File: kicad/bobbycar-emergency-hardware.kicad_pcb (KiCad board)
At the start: 2 copper layers, 40 x 90 mm, 44 parts, among them J1 CAN2, J2 PROG, Q1 SS8050_C2150, Q2 SS8050_C2150, SW1 ANALOG_LEFT, U1 SN65HVD231, U2 ESP32-WROOM-32, U3 AMS1117-3.3, U4 MPM2359, U5 CH343G

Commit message: PCB Files and more screenshots
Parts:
- removed G***: LOGO, Logo:lenas_bobbycar_logo

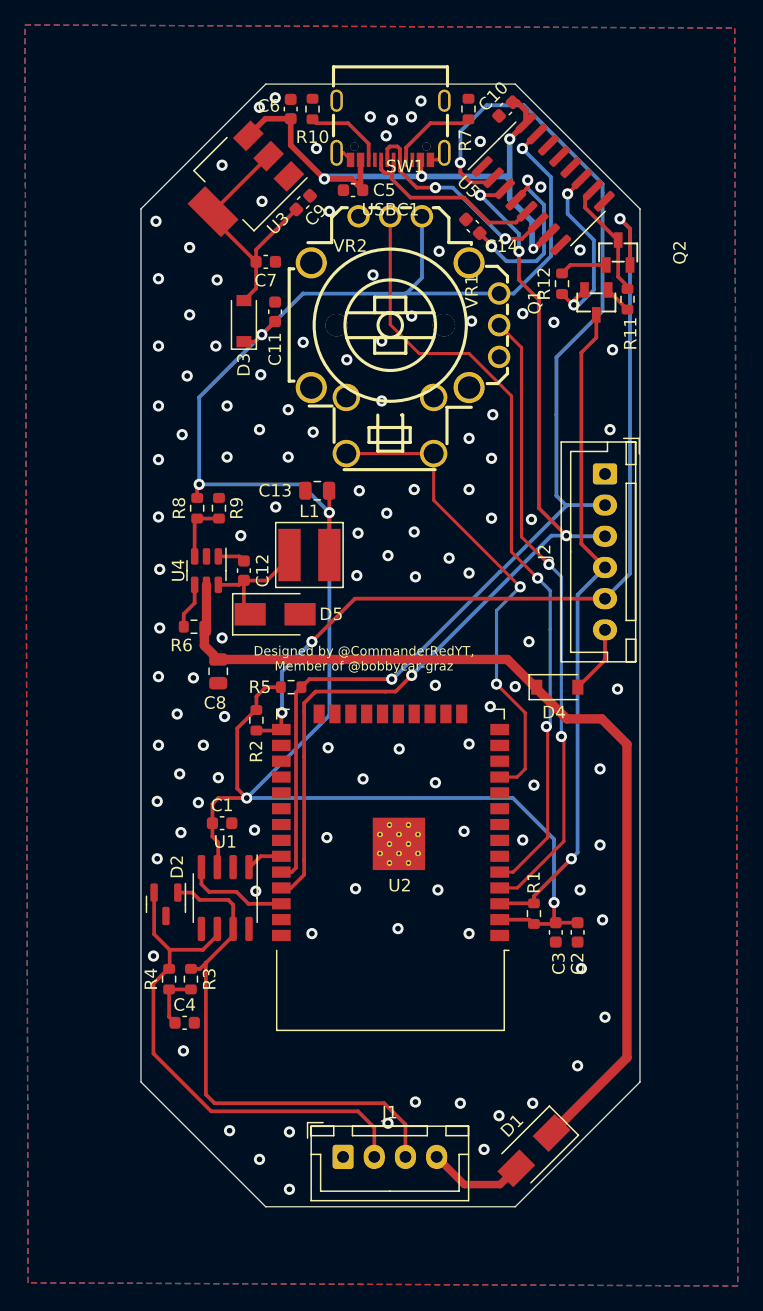
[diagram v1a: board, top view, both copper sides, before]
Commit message: Fixed JLCPCB, added marks for orientation etc
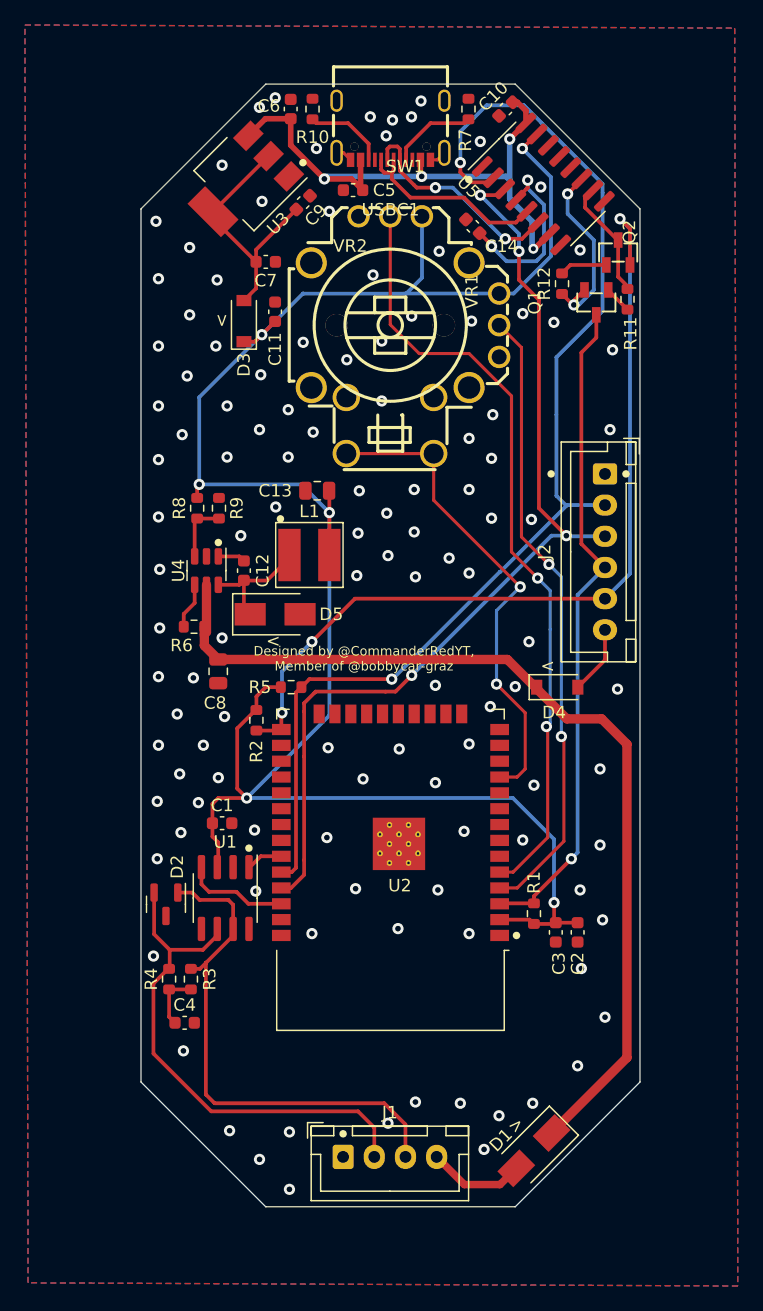
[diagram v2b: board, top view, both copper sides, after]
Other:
- board text added: ">"
